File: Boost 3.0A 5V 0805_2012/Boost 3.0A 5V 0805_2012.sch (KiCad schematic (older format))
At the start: 14 parts

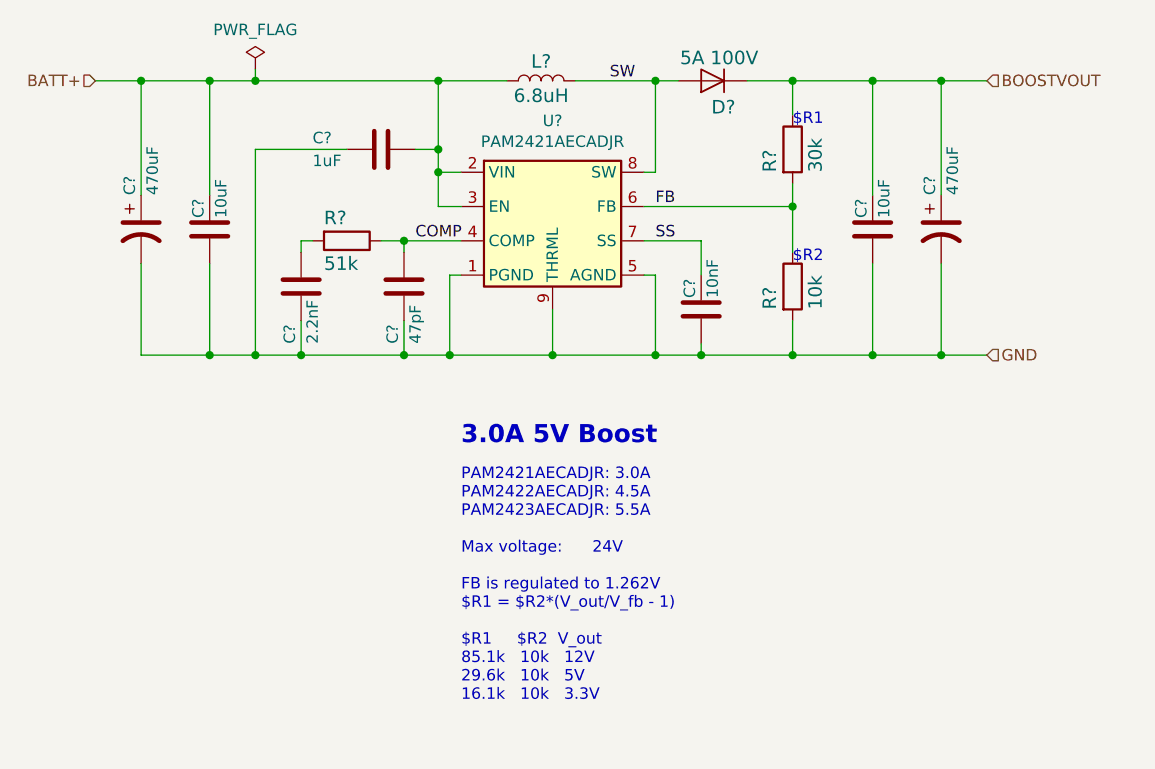
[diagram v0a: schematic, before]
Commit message: Updated Li-Ion schematics
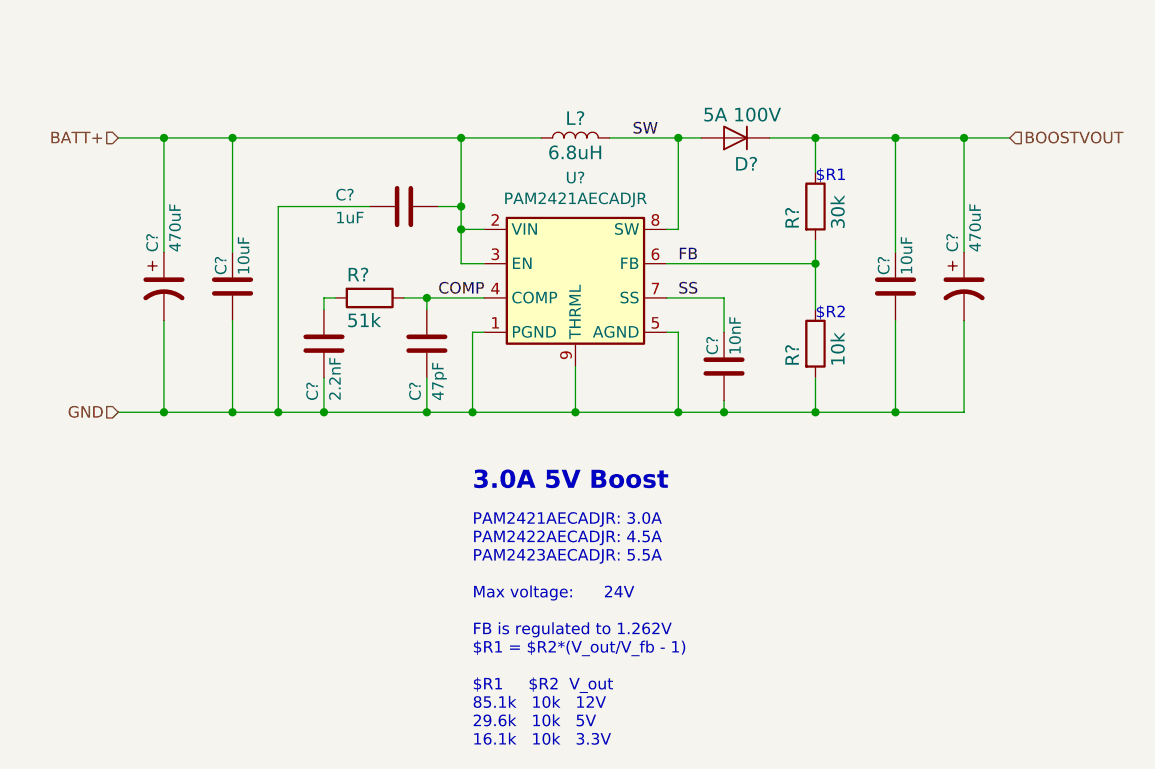
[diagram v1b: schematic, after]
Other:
- moved on the sheet: C?, D?, L?, R?, U?
